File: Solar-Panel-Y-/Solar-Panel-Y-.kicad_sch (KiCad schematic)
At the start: 75 parts, among them J1 FTS-105-01-L-DV-A, J2 BM02B-SRSS-TB, Q1 BSS138DWQ-7, Q2 MBT2222ADW1T1, Q3 BSS138DWQ-7, Q4 MBT2222ADW1T1, SW1 SW_SPDT, SW2 SW_SPDT, U1 BQ25570RGRR, U2 TSL2561

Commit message: New Y- Layout
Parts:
- added SC3, SC7: SolarCell_Small, solarpanels:KXOB25-05X3F, symbol solarpanels:SolarCell_Small
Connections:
- net GND: now also SC3.2 (V-)
- net VSOLAR_FULL: now also SC7.1 (V+)
- net at D3.1 (K), D4.2 (A), SC1.1 (V+)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: now also SC3.1 (V+), SC7.2 (V-)
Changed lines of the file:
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@@
   (junction (at 270.256 70.485) (diameter 0) (color 0 0 0 0)
   )
+  (junction (at 237.236 89.408) (diameter 0) (color 0 0 0 0)
+  )
   (junction (at 431.673 51.435) (diameter 0) (color 0 0 0 0)
   )
@@
   (junction (at 64.008 109.22) (diameter 0) (color 0 0 0 0)
   )
+  (junction (at 312.547 89.408) (diameter 0) (color 0 0 0 0)
+  )
   (junction (at 431.673 89.535) (diameter 0) (color 0 0 0 0)
   )
@@
   (junction (at 416.433 76.835) (diameter 0) (color 0 0 0 0)
   )
+  (junction (at 270.256 89.408) (diameter 0) (color 0 0 0 0)
+  )
   (junction (at 51.308 50.8) (diameter 0) (color 0 0 0 0)
   )
@@
   (junction (at 80.518 81.28) (diameter 0) (color 0 0 0 0)
   )
+  (junction (at 279.527 89.408) (diameter 0) (color 0 0 0 0)
+  )
   (junction (at 64.008 120.65) (diameter 0) (color 0 0 0 0)
   )
@@
     (stroke (width 0) (type default) (color 0 0 0 0))
   )
-  (wire (pts (xy 312.547 70.485) (xy 312.547 108.585))
+  (wire (pts (xy 312.547 70.485) (xy 312.547 89.408))
     (stroke (width 0) (type default) (color 0 0 0 0))
   )
@@
     (stroke (width 0) (type default) (color 0 0 0 0))
   )
-  (wire (pts (xy 270.256 70.485) (xy 270.256 108.585))
+  (wire (pts (xy 270.256 70.485) (xy 270.256 89.408))
     (stroke (width 0) (type default) (color 0 0 0 0))
   )
@@
     (stroke (width 0) (type default) (color 0 0 0 0))
   )
+  (wire (pts (xy 279.527 89.408) (xy 279.527 108.585))
+    (stroke (width 0) (type default) (color 0 0 0 0))
+  )
   (wire (pts (xy 434.213 60.325) (xy 431.673 60.325))
     (stroke (width 0) (type default) (color 0 0 0 0))
@@
     (stroke (width 0) (type default) (color 0 0 0 0))
   )
+  (wire (pts (xy 312.547 89.408) (xy 312.547 108.585))
+    (stroke (width 0) (type default) (color 0 0 0 0))
+  )
   (wire (pts (xy 36.322 165.227) (xy 36.322 167.767))
     (stroke (width 0) (type default) (color 0 0 0 0))
@@
     (stroke (width 0) (type default) (color 0 0 0 0))
   )
-  (wire (pts (xy 279.527 70.485) (xy 279.527 108.585))
+  (wire (pts (xy 279.527 70.485) (xy 279.527 89.408))
     (stroke (width 0) (type default) (color 0 0 0 0))
   )
@@
     (stroke (width 0) (type default) (color 0 0 0 0))
   )
-  (wire (pts (xy 237.236 70.485) (xy 237.236 108.585))
+  (wire (pts (xy 237.236 70.485) (xy 237.236 89.408))
     (stroke (width 0) (type default) (color 0 0 0 0))
   )
@@
     (stroke (width 0) (type default) (color 0 0 0 0))
   )
+  (wire (pts (xy 237.236 89.408) (xy 237.236 108.585))
+    (stroke (width 0) (type default) (color 0 0 0 0))
+  )
   (wire (pts (xy 42.418 66.04) (xy 51.308 66.04))
     (stroke (width 0) (type default) (color 0 0 0 0))
@@
     (stroke (width 0) (type default) (color 0 0 0 0))
   )
+  (wire (pts (xy 270.256 89.408) (xy 270.256 108.585))
+    (stroke (width 0) (type default) (color 0 0 0 0))
+  )
   (wire (pts (xy 169.418 52.07) (xy 169.418 49.53))
     (stroke (width 0) (type default) (color 0 0 0 0))
@@
     (pin "2")
   )
+  (symbol (lib_id "solarpanels:SolarCell_Small") (at 253.746 89.408 0) (mirror y) (unit 1)
+    (in_bom yes) (on_board yes)
+    (property "Reference" "SC3" (id 0) (at 253.746 80.137 0))
+    (property "Value" "SolarCell_Small" (id 1) (at 253.746 82.4484 0))
+    (property "Footprint" "solarpanels:KXOB25-05X3F" (id 2) (at 253.746 83.058 0)
+      (effects (font (size 1.27 1.27)) hide)
+    )
+    (property "Datasheet" "" (id 3) (at 248.666 89.408 90)
+      (effects (font (size 1.27 1.27)) hide)
+    )
+    (pin "1")
+    (pin "2")
+  )
   (symbol (lib_id "power:GND") (at 431.673 89.535 0) (unit 1)
     (in_bom yes) (on_board yes)
@@
     (pin "1")
   )
+  (symbol (lib_id "solarpanels:SolarCell_Small") (at 296.037 89.408 0) (mirror y) (unit 1)
+    (in_bom yes) (on_board yes)
+    (property "Reference" "SC7" (id 0) (at 296.037 80.137 0))
+    (property "Value" "SolarCell_Small" (id 1) (at 296.037 82.4484 0))
+    (property "Footprint" "solarpanels:KXOB25-05X3F" (id 2) (at 296.037 83.058 0)
+      (effects (font (size 1.27 1.27)) hide)
+    )
+    (property "Datasheet" "" (id 3) (at 290.957 89.408 90)
+      (effects (font (size 1.27 1.27)) hide)
+    )
+    (pin "1")
+    (pin "2")
+  )
   (symbol (lib_id "Device:C") (at 389.763 85.725 0) (unit 1)
     (in_bom yes) (on_board yes)
@@
       (reference "SC2") (unit 1) (value "SolarCell_Small") (footprint "solarpanels:KXOB25-05X3F")
     )
+    (path "/56135c31-39d5-4bf4-8a21-a5907a5cb015"
+      (reference "SC3") (unit 1) (value "SolarCell_Small") (footprint "solarpanels:KXOB25-05X3F")
+    )
     (path "/b89143dc-9d73-4565-ad22-5ae64488744a"
       (reference "SC4") (unit 1) (value "SolarCell_Small") (footprint "solarpanels:KXOB25-05X3F")
@@
       (reference "SC6") (unit 1) (value "SolarCell_Small") (footprint "solarpanels:KXOB25-05X3F")
     )
+    (path "/9b814b93-df8a-4a89-8493-dd2d4c779c55"
+      (reference "SC7") (unit 1) (value "SolarCell_Small") (footprint "solarpanels:KXOB25-05X3F")
+    )
     (path "/f0d7e97a-a264-4327-8ec7-c519407852f5"

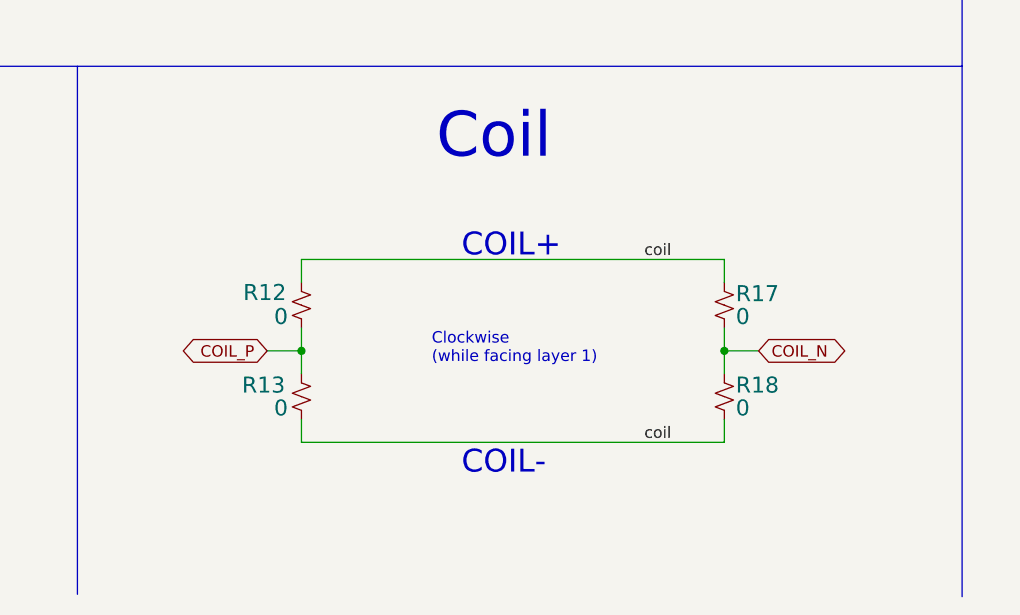
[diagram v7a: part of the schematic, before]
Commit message: Modified coil resistors on Y- board
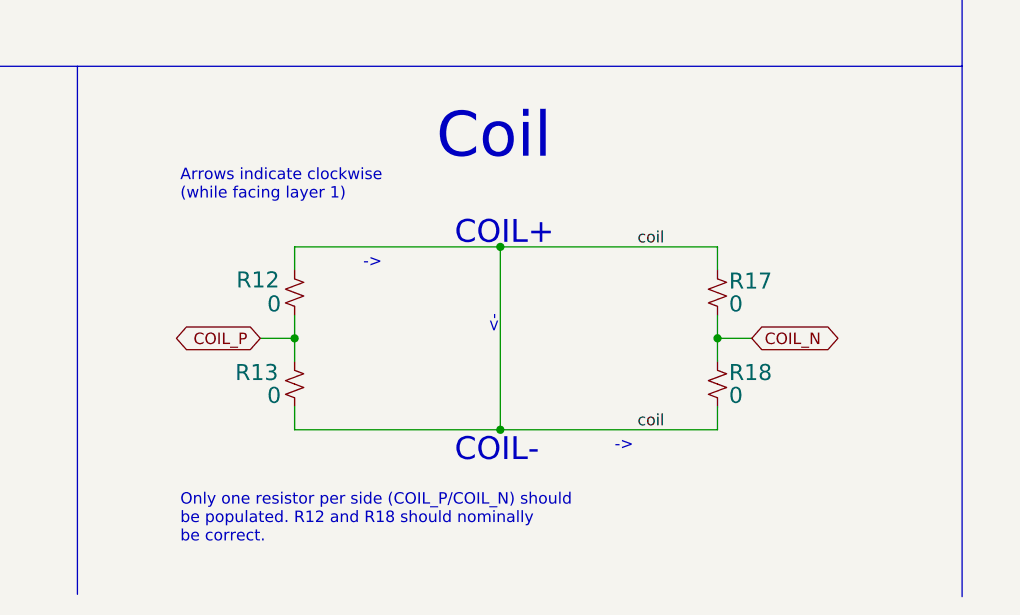
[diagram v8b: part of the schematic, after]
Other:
- note added: "->"
- note added: "<-"
- note added: "Arrows indicate clockwise (while facing layer 1)"
- note added: "Only one resistor per side (COIL_P/COIL_N) should be populated. R12 and R18 should nominally be correct."
- note removed: "Clockwise (while facing layer 1)"
- moved on the sheet: R12, R13, R17, R18
